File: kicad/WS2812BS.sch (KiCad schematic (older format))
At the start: 18 parts

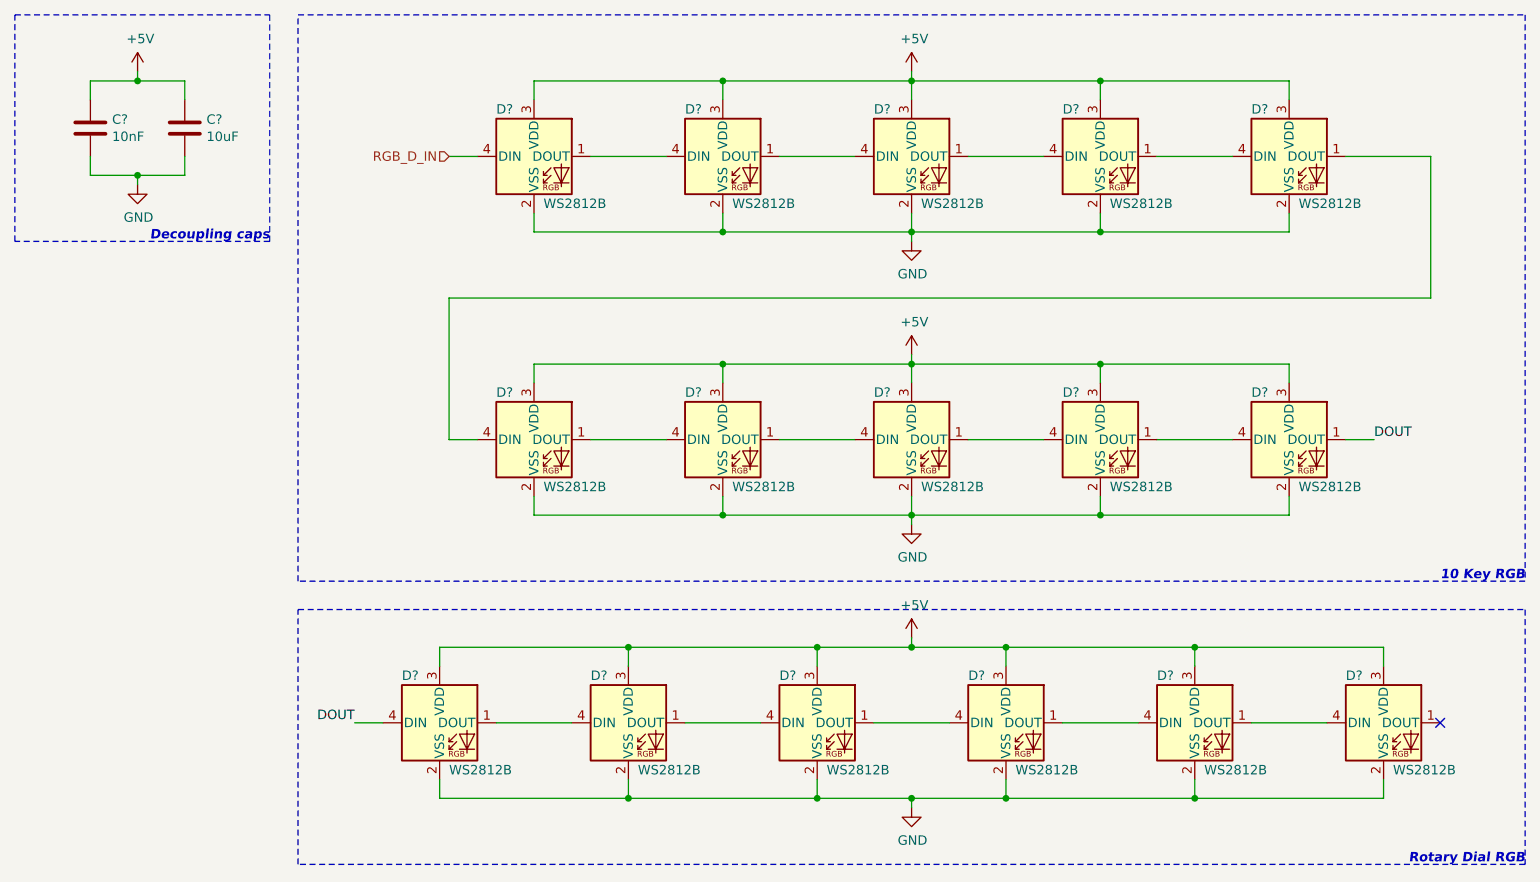
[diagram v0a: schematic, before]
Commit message: Updated labels and added footprints
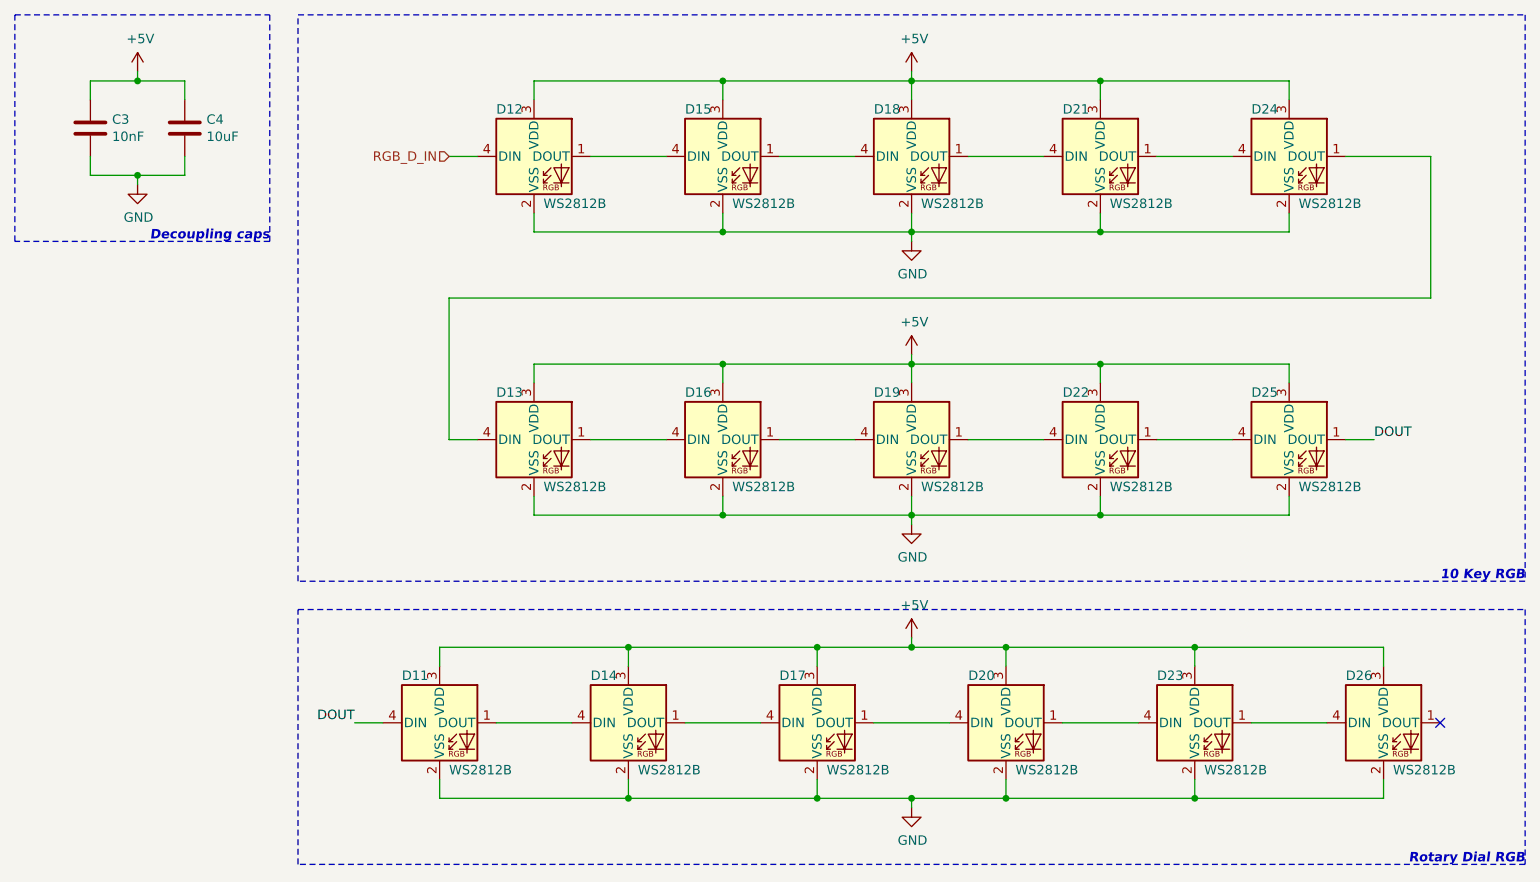
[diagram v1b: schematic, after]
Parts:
- C3, C4: renamed from C?; footprint (none) -> Capacitor_SMD:C_1206_3216Metric_Pad1.33x1.80mm_HandSolder
- gave numbers to parts that had none: 16
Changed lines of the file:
@@
 $EndDescr
 $Comp
-L LED:WS2812B D?
+L LED:WS2812B D12
 U 1 1 6098DF2D
 P 3750 2250
-F 0 "D?" H 3550 2500 50  0000 L CNN
+F 0 "D12" H 3550 2500 50  0000 L CNN
 F 1 "WS2812B" H 3800 2000 50  0000 L CNN
 F 2 "LED_SMD:LED_WS2812B_PLCC4_5.0x5.0mm_P3.2mm" H 3800 1950 50  0001 L TNN
@@
 $EndComp
 $Comp
-L LED:WS2812B D?
+L LED:WS2812B D15
 U 1 1 6098EF11
 P 4750 2250
-F 0 "D?" H 4550 2500 50  0000 L CNN
+F 0 "D15" H 4550 2500 50  0000 L CNN
 F 1 "WS2812B" H 4800 2000 50  0000 L CNN
 F 2 "LED_SMD:LED_WS2812B_PLCC4_5.0x5.0mm_P3.2mm" H 4800 1950 50  0001 L TNN
@@
 $EndComp
 $Comp
-L LED:WS2812B D?
+L LED:WS2812B D18
 U 1 1 6098F421
 P 5750 2250
-F 0 "D?" H 5550 2500 50  0000 L CNN
+F 0 "D18" H 5550 2500 50  0000 L CNN
 F 1 "WS2812B" H 5800 2000 50  0000 L CNN
 F 2 "LED_SMD:LED_WS2812B_PLCC4_5.0x5.0mm_P3.2mm" H 5800 1950 50  0001 L TNN
@@
 $EndComp
 $Comp
-L LED:WS2812B D?
+L LED:WS2812B D21
 U 1 1 6098F97F
 P 6750 2250
-F 0 "D?" H 6550 2500 50  0000 L CNN
+F 0 "D21" H 6550 2500 50  0000 L CNN
 F 1 "WS2812B" H 6800 2000 50  0000 L CNN
 F 2 "LED_SMD:LED_WS2812B_PLCC4_5.0x5.0mm_P3.2mm" H 6800 1950 50  0001 L TNN
@@
 $EndComp
 $Comp
-L LED:WS2812B D?
+L LED:WS2812B D24
 U 1 1 6098FE01
 P 7750 2250
-F 0 "D?" H 7550 2500 50  0000 L CNN
+F 0 "D24" H 7550 2500 50  0000 L CNN
 F 1 "WS2812B" H 7800 2000 50  0000 L CNN
 F 2 "LED_SMD:LED_WS2812B_PLCC4_5.0x5.0mm_P3.2mm" H 7800 1950 50  0001 L TNN
@@
 	7050 2250 7450 2250
 $Comp
-L LED:WS2812B D?
+L LED:WS2812B D13
 U 1 1 609983F4
 P 3750 3750
-F 0 "D?" H 3550 4000 50  0000 L CNN
+F 0 "D13" H 3550 4000 50  0000 L CNN
 F 1 "WS2812B" H 3800 3500 50  0000 L CNN
 F 2 "LED_SMD:LED_WS2812B_PLCC4_5.0x5.0mm_P3.2mm" H 3800 3450 50  0001 L TNN
@@
 $EndComp
 $Comp
-L LED:WS2812B D?
+L LED:WS2812B D16
 U 1 1 609984C6
 P 4750 3750
-F 0 "D?" H 4550 4000 50  0000 L CNN
+F 0 "D16" H 4550 4000 50  0000 L CNN
 F 1 "WS2812B" H 4800 3500 50  0000 L CNN
 F 2 "LED_SMD:LED_WS2812B_PLCC4_5.0x5.0mm_P3.2mm" H 4800 3450 50  0001 L TNN
@@
 $EndComp
 $Comp
-L LED:WS2812B D?
+L LED:WS2812B D19
 U 1 1 609984D0
 P 5750 3750
-F 0 "D?" H 5550 4000 50  0000 L CNN
+F 0 "D19" H 5550 4000 50  0000 L CNN
 F 1 "WS2812B" H 5800 3500 50  0000 L CNN
 F 2 "LED_SMD:LED_WS2812B_PLCC4_5.0x5.0mm_P3.2mm" H 5800 3450 50  0001 L TNN
@@
 $EndComp
 $Comp
-L LED:WS2812B D?
+L LED:WS2812B D22
 U 1 1 609984DA
 P 6750 3750
-F 0 "D?" H 6550 4000 50  0000 L CNN
+F 0 "D22" H 6550 4000 50  0000 L CNN
 F 1 "WS2812B" H 6800 3500 50  0000 L CNN
 F 2 "LED_SMD:LED_WS2812B_PLCC4_5.0x5.0mm_P3.2mm" H 6800 3450 50  0001 L TNN
@@
 $EndComp
 $Comp
-L LED:WS2812B D?
+L LED:WS2812B D25
 U 1 1 609984E4
 P 7750 3750
-F 0 "D?" H 7550 4000 50  0000 L CNN
+F 0 "D25" H 7550 4000 50  0000 L CNN
 F 1 "WS2812B" H 7800 3500 50  0000 L CNN
 F 2 "LED_SMD:LED_WS2812B_PLCC4_5.0x5.0mm_P3.2mm" H 7800 3450 50  0001 L TNN
@@
 	7050 3750 7450 3750
 $Comp
-L power:+5V #PWR?
+L power:+5V #PWR019
 U 1 1 609A38E2
 P 5750 1800
-F 0 "#PWR?" H 5750 1650 50  0001 C CNN
+F 0 "#PWR019" H 5750 1650 50  0001 C CNN
 F 1 "+5V" H 5765 1973 50  0000 C CNN
 F 2 "" H 5750 1800 50  0001 C CNN
@@
 Connection ~ 6750 1850
 $Comp
-L power:+5V #PWR?
+L power:+5V #PWR021
 U 1 1 609A4E49
 P 5750 3300
-F 0 "#PWR?" H 5750 3150 50  0001 C CNN
+F 0 "#PWR021" H 5750 3150 50  0001 C CNN
 F 1 "+5V" H 5765 3473 50  0000 C CNN
 F 2 "" H 5750 3300 50  0001 C CNN
@@
 Connection ~ 4750 3350
 $Comp
-L power:GND #PWR?
+L power:GND #PWR020
 U 1 1 609A7BDB
 P 5750 2700
-F 0 "#PWR?" H 5750 2450 50  0001 C CNN
+F 0 "#PWR020" H 5750 2450 50  0001 C CNN
 F 1 "GND" H 5755 2527 50  0000 C CNN
 F 2 "" H 5750 2700 50  0001 C CNN
@@
 Connection ~ 6750 2650
 $Comp
-L power:GND #PWR?
+L power:GND #PWR022
 U 1 1 609AA9BE
 P 5750 4200
-F 0 "#PWR?" H 5750 3950 50  0001 C CNN
+F 0 "#PWR022" H 5750 3950 50  0001 C CNN
 F 1 "GND" H 5755 4027 50  0000 C CNN
 F 2 "" H 5750 4200 50  0001 C CNN
@@
 10 Key RGB
 $Comp
-L LED:WS2812B D?
+L LED:WS2812B D11
 U 1 1 609B1E57
 P 3250 5250
-F 0 "D?" H 3050 5500 50  0000 L CNN
+F 0 "D11" H 3050 5500 50  0000 L CNN
 F 1 "WS2812B" H 3300 5000 50  0000 L CNN
 F 2 "LED_SMD:LED_WS2812B_PLCC4_5.0x5.0mm_P3.2mm" H 3300 4950 50  0001 L TNN
@@
 $EndComp
 $Comp
-L LED:WS2812B D?
+L LED:WS2812B D14
 U 1 1 609B30CE
 P 4250 5250
-F 0 "D?" H 4050 5500 50  0000 L CNN
+F 0 "D14" H 4050 5500 50  0000 L CNN
 F 1 "WS2812B" H 4300 5000 50  0000 L CNN
 F 2 "LED_SMD:LED_WS2812B_PLCC4_5.0x5.0mm_P3.2mm" H 4300 4950 50  0001 L TNN
@@
 $EndComp
 $Comp
-L LED:WS2812B D?
+L LED:WS2812B D17
 U 1 1 609B3913
 P 5250 5250
-F 0 "D?" H 5050 5500 50  0000 L CNN
+F 0 "D17" H 5050 5500 50  0000 L CNN
 F 1 "WS2812B" H 5300 5000 50  0000 L CNN
 F 2 "LED_SMD:LED_WS2812B_PLCC4_5.0x5.0mm_P3.2mm" H 5300 4950 50  0001 L TNN
@@
 $EndComp
 $Comp
-L LED:WS2812B D?
+L LED:WS2812B D20
 U 1 1 609B4099
 P 6250 5250
-F 0 "D?" H 6050 5500 50  0000 L CNN
+F 0 "D20" H 6050 5500 50  0000 L CNN
 F 1 "WS2812B" H 6300 5000 50  0000 L CNN
 F 2 "LED_SMD:LED_WS2812B_PLCC4_5.0x5.0mm_P3.2mm" H 6300 4950 50  0001 L TNN
@@
 $EndComp
 $Comp
-L LED:WS2812B D?
+L LED:WS2812B D23
 U 1 1 609B4953
 P 7250 5250
-F 0 "D?" H 7050 5500 50  0000 L CNN
+F 0 "D23" H 7050 5500 50  0000 L CNN
 F 1 "WS2812B" H 7300 5000 50  0000 L CNN
 F 2 "LED_SMD:LED_WS2812B_PLCC4_5.0x5.0mm_P3.2mm" H 7300 4950 50  0001 L TNN
@@
 $EndComp
 $Comp
-L LED:WS2812B D?
+L LED:WS2812B D26
 U 1 1 609B4F92
 P 8250 5250
-F 0 "D?" H 8050 5500 50  0000 L CNN
+F 0 "D26" H 8050 5500 50  0000 L CNN
 F 1 "WS2812B" H 8300 5000 50  0000 L CNN
 F 2 "LED_SMD:LED_WS2812B_PLCC4_5.0x5.0mm_P3.2mm" H 8300 4950 50  0001 L TNN
@@
 NoConn ~ 8550 5250
 $Comp
-L power:+5V #PWR?
+L power:+5V #PWR023
 U 1 1 609C0561
 P 5750 4800
-F 0 "#PWR?" H 5750 4650 50  0001 C CNN
+F 0 "#PWR023" H 5750 4650 50  0001 C CNN
 F 1 "+5V" H 5765 4973 50  0000 C CNN
 F 2 "" H 5750 4800 50  0001 C CNN
@@
 Connection ~ 7250 4850
 $Comp
-L power:GND #PWR?
+L power:GND #PWR024
 U 1 1 609C977F
 P 5750 5700
-F 0 "#PWR?" H 5750 5450 50  0001 C CNN
+F 0 "#PWR024" H 5750 5450 50  0001 C CNN
 F 1 "GND" H 5755 5527 50  0000 C CNN
 F 2 "" H 5750 5700 50  0001 C CNN
@@
 Rotary Dial RGB
 $Comp
-L Device:C C?
+L Device:C C3
 U 1 1 609D8366
 P 1400 2100
-F 0 "C?" H 1515 2146 50  0000 L CNN
+F 0 "C3" H 1515 2146 50  0000 L CNN
 F 1 "10nF" H 1515 2055 50  0000 L CNN
-F 2 "" H 1438 1950 50  0001 C CNN
+F 2 "Capacitor_SMD:C_1206_3216Metric_Pad1.33x1.80mm_HandSolder" H 1438 1950 50  0001 C CNN
 F 3 "~" H 1400 2100 50  0001 C CNN
 	1    1400 2100
@@
 $EndComp
 $Comp
-L Device:C C?
+L Device:C C4
 U 1 1 609D9203
 P 1900 2100
-F 0 "C?" H 2015 2146 50  0000 L CNN
+F 0 "C4" H 2015 2146 50  0000 L CNN
 F 1 "10uF" H 2015 2055 50  0000 L CNN
-F 2 "" H 1938 1950 50  0001 C CNN
+F 2 "Capacitor_SMD:C_1206_3216Metric_Pad1.33x1.80mm_HandSolder" H 1938 1950 50  0001 C CNN
 F 3 "~" H 1900 2100 50  0001 C CNN
 	1    1900 2100
@@
 $EndComp
 $Comp
-L power:GND #PWR?
+L power:GND #PWR018
 U 1 1 609D957F
 P 1650 2400
-F 0 "#PWR?" H 1650 2150 50  0001 C CNN
+F 0 "#PWR018" H 1650 2150 50  0001 C CNN
 F 1 "GND" H 1655 2227 50  0000 C CNN
 F 2 "" H 1650 2400 50  0001 C CNN
@@
 $EndComp
 $Comp
-L power:+5V #PWR?
+L power:+5V #PWR017
 U 1 1 609D99B0
 P 1650 1800
-F 0 "#PWR?" H 1650 1650 50  0001 C CNN
+F 0 "#PWR017" H 1650 1650 50  0001 C CNN
 F 1 "+5V" H 1665 1973 50  0000 C CNN
 F 2 "" H 1650 1800 50  0001 C CNN

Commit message: PCB Work
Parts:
- removed D26: WS2812B, LED_SMD:LED_WS2812B_PLCC4_5.0x5.0mm_P3.2mm, symbol LED:WS2812B
- added J3: Conn_01x03, Connector_PinHeader_2.54mm:PinHeader_1x03_P2.54mm_Horizontal, symbol Connector_Generic:Conn_01x03
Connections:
- net +5V: now also J3.1 (Pin_1)
- net GND: now also J3.3 (Pin_3)
- net at D23.1 (DOUT): now also J3.2 (Pin_2)
- net DOUT: no longer names the net of D11.4 (DIN), D25.1 (DOUT)
- no-connect marks 1 -> 0
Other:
- note added: "Backlight RGB"
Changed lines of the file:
@@
 Text Notes 9000 4500 2    50   Italic 10
 10 Key RGB
-$Comp
-L LED:WS2812B D11
-U 1 1 609B1E57
-P 3250 5250
-F 0 "D11" H 3050 5500 50  0000 L CNN
-F 1 "WS2812B" H 3300 5000 50  0000 L CNN
-F 2 "LED_SMD:LED_WS2812B_PLCC4_5.0x5.0mm_P3.2mm" H 3300 4950 50  0001 L TNN
-F 3 "https://cdn-shop.adafruit.com/datasheets/WS2812B.pdf" H 3350 4875 50  0001 L TNN
-	1    3250 5250
-	1    0    0    -1
-$EndComp
-$Comp
-L LED:WS2812B D14
-U 1 1 609B30CE
-P 4250 5250
-F 0 "D14" H 4050 5500 50  0000 L CNN
-F 1 "WS2812B" H 4300 5000 50  0000 L CNN
-F 2 "LED_SMD:LED_WS2812B_PLCC4_5.0x5.0mm_P3.2mm" H 4300 4950 50  0001 L TNN
-F 3 "https://cdn-shop.adafruit.com/datasheets/WS2812B.pdf" H 4350 4875 50  0001 L TNN
-	1    4250 5250
-	1    0    0    -1
-$EndComp
-$Comp
-L LED:WS2812B D17
-U 1 1 609B3913
-P 5250 5250
-F 0 "D17" H 5050 5500 50  0000 L CNN
-F 1 "WS2812B" H 5300 5000 50  0000 L CNN
-F 2 "LED_SMD:LED_WS2812B_PLCC4_5.0x5.0mm_P3.2mm" H 5300 4950 50  0001 L TNN
-F 3 "https://cdn-shop.adafruit.com/datasheets/WS2812B.pdf" H 5350 4875 50  0001 L TNN
-	1    5250 5250
-	1    0    0    -1
-$EndComp
-$Comp
-L LED:WS2812B D20
-U 1 1 609B4099
-P 6250 5250
-F 0 "D20" H 6050 5500 50  0000 L CNN
-F 1 "WS2812B" H 6300 5000 50  0000 L CNN
-F 2 "LED_SMD:LED_WS2812B_PLCC4_5.0x5.0mm_P3.2mm" H 6300 4950 50  0001 L TNN
-F 3 "https://cdn-shop.adafruit.com/datasheets/WS2812B.pdf" H 6350 4875 50  0001 L TNN
-	1    6250 5250
-	1    0    0    -1
-$EndComp
-$Comp
-L LED:WS2812B D23
-U 1 1 609B4953
-P 7250 5250
-F 0 "D23" H 7050 5500 50  0000 L CNN
-F 1 "WS2812B" H 7300 5000 50  0000 L CNN
-F 2 "LED_SMD:LED_WS2812B_PLCC4_5.0x5.0mm_P3.2mm" H 7300 4950 50  0001 L TNN
-F 3 "https://cdn-shop.adafruit.com/datasheets/WS2812B.pdf" H 7350 4875 50  0001 L TNN
-	1    7250 5250
-	1    0    0    -1
-$EndComp
-$Comp
-L LED:WS2812B D26
-U 1 1 609B4F92
-P 8250 5250
-F 0 "D26" H 8050 5500 50  0000 L CNN
-F 1 "WS2812B" H 8300 5000 50  0000 L CNN
-F 2 "LED_SMD:LED_WS2812B_PLCC4_5.0x5.0mm_P3.2mm" H 8300 4950 50  0001 L TNN
-F 3 "https://cdn-shop.adafruit.com/datasheets/WS2812B.pdf" H 8350 4875 50  0001 L TNN
-	1    8250 5250
-	1    0    0    -1
-$EndComp
-Text Label 8200 3750 0    50   ~ 0
-DOUT
-Wire Wire Line
-	8200 3750 8050 3750
-Text Label 2800 5250 2    50   ~ 0
-DOUT
-Wire Wire Line
-	2800 5250 2950 5250
-Wire Wire Line
-	3550 5250 3950 5250
-Wire Wire Line
-	4550 5250 4950 5250
-Wire Wire Line
-	5550 5250 5950 5250
-Wire Wire Line
-	6550 5250 6950 5250
-Wire Wire Line
-	7550 5250 7950 5250
-NoConn ~ 8550 5250
-$Comp
-L power:+5V #PWR023
-U 1 1 609C0561
-P 5750 4800
-F 0 "#PWR023" H 5750 4650 50  0001 C CNN
-F 1 "+5V" H 5765 4973 50  0000 C CNN
-F 2 "" H 5750 4800 50  0001 C CNN
-F 3 "" H 5750 4800 50  0001 C CNN
-	1    5750 4800
-	1    0    0    -1
-$EndComp
-Wire Wire Line
-	6250 4950 6250 4850
-Wire Wire Line
-	6250 4850 5750 4850
-Wire Wire Line
-	5750 4850 5750 4800
-Wire Wire Line
-	5250 4950 5250 4850
-Wire Wire Line
-	5250 4850 5750 4850
-Connection ~ 5750 4850
-Wire Wire Line
-	4250 4950 4250 4850
-Wire Wire Line
-	4250 4850 5250 4850
-Connection ~ 5250 4850
-Wire Wire Line
-	3250 4950 3250 4850
-Wire Wire Line
-	3250 4850 4250 4850
-Connection ~ 4250 4850
-Wire Wire Line
-	7250 4950 7250 4850
-Wire Wire Line
-	7250 4850 6250 4850
-Connection ~ 6250 4850
-Wire Wire Line
-	8250 4950 8250 4850
-Wire Wire Line
-	8250 4850 7250 4850
-Connection ~ 7250 4850
-$Comp
-L power:GND #PWR024
-U 1 1 609C977F
-P 5750 5700
-F 0 "#PWR024" H 5750 5450 50  0001 C CNN
-F 1 "GND" H 5755 5527 50  0000 C CNN
-F 2 "" H 5750 5700 50  0001 C CNN
-F 3 "" H 5750 5700 50  0001 C CNN
-	1    5750 5700
-	1    0    0    -1
-$EndComp
-Wire Wire Line
-	5250 5550 5250 5650
-Wire Wire Line
-	5250 5650 5750 5650
-Wire Wire Line
-	5750 5650 5750 5700
-Wire Wire Line
-	6250 5550 6250 5650
-Wire Wire Line
-	6250 5650 5750 5650
-Connection ~ 5750 5650
-Wire Wire Line
-	7250 5550 7250 5650
-Wire Wire Line
-	7250 5650 6250 5650
-Connection ~ 6250 5650
-Wire Wire Line
-	8250 5550 8250 5650
-Wire Wire Line
-	8250 5650 7250 5650
-Connection ~ 7250 5650
-Wire Wire Line
-	4250 5550 4250 5650
-Wire Wire Line
-	4250 5650 5250 5650
-Connection ~ 5250 5650
-Wire Wire Line
-	3250 5550 3250 5650
-Wire Wire Line
-	3250 5650 4250 5650
-Connection ~ 4250 5650
-Wire Notes Line
-	2500 4650 9000 4650
 Wire Notes Line
 	9000 4650 9000 6000
 Wire Notes Line
-	9000 6000 2500 6000
-Wire Notes Line
-	2500 6000 2500 4650
+	7500 6000 7500 4650
 Text Notes 9000 6000 2    50   Italic 10
 Rotary Dial RGB
@@
 Text Notes 2350 2700 2    50   Italic 10
 Decoupling caps\n
+$Comp
+L Connector_Generic:Conn_01x03 J3
+U 1 1 60A60470
+P 8400 5300
+F 0 "J3" H 8480 5342 50  0000 L CNN
+F 1 "Conn_01x03" H 8480 5251 50  0000 L CNN
+F 2 "Connector_PinHeader_2.54mm:PinHeader_1x03_P2.54mm_Horizontal" H 8400 5300 50  0001 C CNN
+F 3 "~" H 8400 5300 50  0001 C CNN
+	1    8400 5300
+	1    0    0    -1
+$EndComp
+$Comp
+L power:+5V #PWR023
+U 1 1 60A6166B
+P 8150 5150
+F 0 "#PWR023" H 8150 5000 50  0001 C CNN
+F 1 "+5V" H 8165 5323 50  0000 C CNN
+F 2 "" H 8150 5150 50  0001 C CNN
+F 3 "" H 8150 5150 50  0001 C CNN
+	1    8150 5150
+	1    0    0    -1
+$EndComp
+$Comp
+L power:GND #PWR024
+U 1 1 60A61D5A
+P 8150 5450
+F 0 "#PWR024" H 8150 5200 50  0001 C CNN
+F 1 "GND" H 8155 5277 50  0000 C CNN
+F 2 "" H 8150 5450 50  0001 C CNN
+F 3 "" H 8150 5450 50  0001 C CNN
+	1    8150 5450
+	1    0    0    -1
+$EndComp
+Wire Wire Line
+	8200 5400 8150 5400
+Wire Wire Line
+	8150 5400 8150 5450
+Wire Wire Line
+	8200 5200 8150 5200
+Wire Wire Line
+	8150 5200 8150 5150
+Wire Notes Line
+	7500 4650 9000 4650
+Wire Notes Line
+	9000 6000 7500 6000
+$Comp
+L LED:WS2812B D11
+U 1 1 60A81918
+P 3000 5300
+F 0 "D11" H 2800 5550 50  0000 L CNN
+F 1 "WS2812B" H 3050 5050 50  0000 L CNN
+F 2 "LED_SMD:LED_WS2812B_PLCC4_5.0x5.0mm_P3.2mm" H 3050 5000 50  0001 L TNN
+F 3 "https://cdn-shop.adafruit.com/datasheets/WS2812B.pdf" H 3100 4925 50  0001 L TNN
+	1    3000 5300
+	1    0    0    -1
+$EndComp
+$Comp
+L LED:WS2812B D14
+U 1 1 60A81B40
+P 4000 5300
+F 0 "D14" H 3800 5550 50  0000 L CNN
+F 1 "WS2812B" H 4050 5050 50  0000 L CNN
+F 2 "LED_SMD:LED_WS2812B_PLCC4_5.0x5.0mm_P3.2mm" H 4050 5000 50  0001 L TNN
+F 3 "https://cdn-shop.adafruit.com/datasheets/WS2812B.pdf" H 4100 4925 50  0001 L TNN
+	1    4000 5300
+	1    0    0    -1
+$EndComp
+$Comp
+L LED:WS2812B D17
+U 1 1 60A81B4A
+P 5000 5300
+F 0 "D17" H 4800 5550 50  0000 L CNN
+F 1 "WS2812B" H 5050 5050 50  0000 L CNN
+F 2 "LED_SMD:LED_WS2812B_PLCC4_5.0x5.0mm_P3.2mm" H 5050 5000 50  0001 L TNN
+F 3 "https://cdn-shop.adafruit.com/datasheets/WS2812B.pdf" H 5100 4925 50  0001 L TNN
+	1    5000 5300
+	1    0    0    -1
+$EndComp
+$Comp
+L LED:WS2812B D20
+U 1 1 60A81B54
+P 6000 5300
+F 0 "D20" H 5800 5550 50  0000 L CNN
+F 1 "WS2812B" H 6050 5050 50  0000 L CNN
+F 2 "LED_SMD:LED_WS2812B_PLCC4_5.0x5.0mm_P3.2mm" H 6050 5000 50  0001 L TNN
+F 3 "https://cdn-shop.adafruit.com/datasheets/WS2812B.pdf" H 6100 4925 50  0001 L TNN
+	1    6000 5300
+	1    0    0    -1
+$EndComp
+$Comp
+L LED:WS2812B D23
+U 1 1 60A81B5E
+P 7000 5300
+F 0 "D23" H 6800 5550 50  0000 L CNN
+F 1 "WS2812B" H 7050 5050 50  0000 L CNN
+F 2 "LED_SMD:LED_WS2812B_PLCC4_5.0x5.0mm_P3.2mm" H 7050 5000 50  0001 L TNN
+F 3 "https://cdn-shop.adafruit.com/datasheets/WS2812B.pdf" H 7100 4925 50  0001 L TNN
+	1    7000 5300
+	1    0    0    -1
+$EndComp
+Wire Wire Line
+	3300 5300 3700 5300
+Wire Wire Line
+	4300 5300 4700 5300
+Wire Wire Line
+	5300 5300 5700 5300
+Wire Wire Line
+	6300 5300 6700 5300
+$Comp
+L power:+5V #PWR025
+U 1 1 60A81B6C
+P 5000 4850
+F 0 "#PWR025" H 5000 4700 50  0001 C CNN
+F 1 "+5V" H 5100 4900 50  0000 C CNN
+F 2 "" H 5000 4850 50  0001 C CNN
+F 3 "" H 5000 4850 50  0001 C CNN
+	1    5000 4850
+	1    0    0    -1
+$EndComp
+Wire Wire Line
+	5000 4850 5000 4900
+Wire Wire Line
+	4000 5000 4000 4900
+Wire Wire Line
+	4000 4900 5000 4900
+Connection ~ 5000 4900
+Wire Wire Line
+	5000 4900 5000 5000
+Wire Wire Line
+	6000 5000 6000 4900
+Wire Wire Line
+	6000 4900 5000 4900
+Wire Wire Line
+	7000 5000 7000 4900
+Wire Wire Line
+	7000 4900 6000 4900
+Connection ~ 6000 4900
+Wire Wire Line
+	3000 5000 3000 4900
+Wire Wire Line
+	3000 4900 4000 4900
+Connection ~ 4000 4900
+$Comp
+L power:GND #PWR026
+U 1 1 60A81B83
+P 5000 5750
+F 0 "#PWR026" H 5000 5500 50  0001 C CNN
+F 1 "GND" H 5005 5577 50  0000 C CNN
+F 2 "" H 5000 5750 50  0001 C CNN
+F 3 "" H 5000 5750 50  0001 C CNN
+	1    5000 5750
+	1    0    0    -1
+$EndComp
+Wire Wire Line
+	5000 5750 5000 5700
+Wire Wire Line
+	4000 5600 4000 5700
+Wire Wire Line
+	4000 5700 5000 5700
+Connection ~ 5000 5700
+Wire Wire Line
+	5000 5700 5000 5600
+Wire Wire Line
+	6000 5600 6000 5700
+Wire Wire Line
+	6000 5700 5000 5700
+Wire Wire Line
+	7000 5600 7000 5700
+Wire Wire Line
+	7000 5700 6000 5700
+Connection ~ 6000 5700
+Wire Wire Line
+	3000 5600 3000 5700
+Wire Wire Line
+	3000 5700 4000 5700
+Connection ~ 4000 5700
+Wire Wire Line
+	8050 3750 8300 3750
+Wire Wire Line
+	8300 3750 8300 4550
+Wire Wire Line
+	8300 4550 2600 4550
+Wire Wire Line
+	2600 4550 2600 5300
+Wire Wire Line
+	2600 5300 2700 5300
+Wire Notes Line
+	2500 4650 7350 4650
+Wire Notes Line
+	7350 4650 7350 6000
+Wire Notes Line
+	7350 6000 2500 6000
+Wire Notes Line
+	2500 6000 2500 4650
+Wire Wire Line
+	7300 5300 8200 5300
+Text Notes 7350 6000 2    50   Italic 10
+Backlight RGB
 $EndSCHEMATC
